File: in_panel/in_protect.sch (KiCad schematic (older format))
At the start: 8 parts

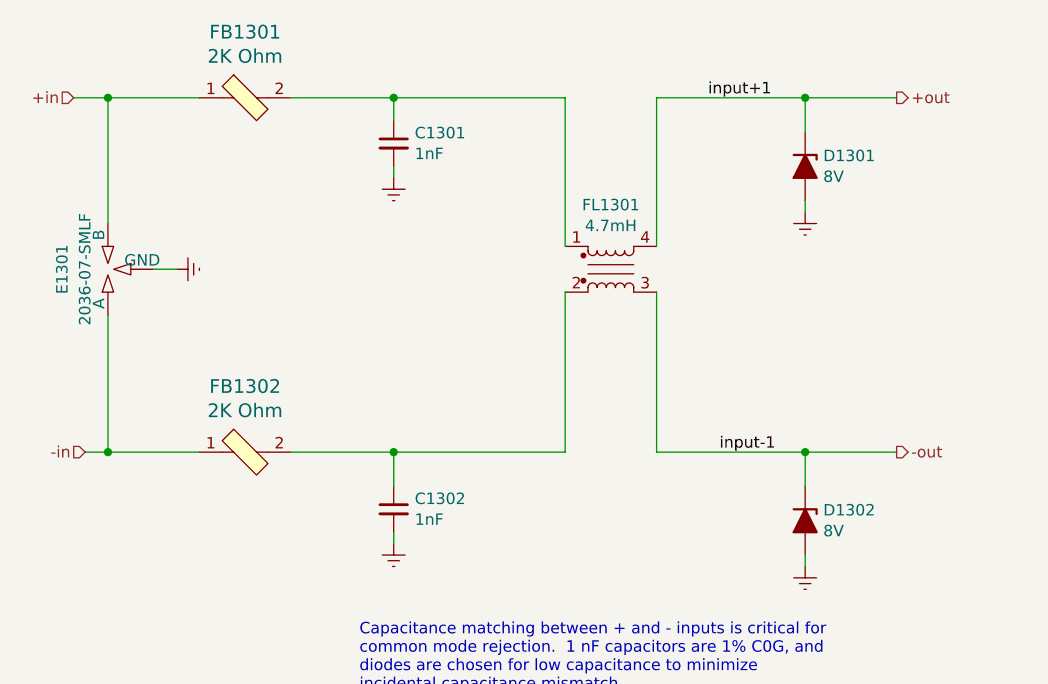
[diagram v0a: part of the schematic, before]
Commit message: More work on in_panel.  Also, shortened input_board by 10mm and tweaked the testpoints a bit, added another GND, and changed the supply TPs to be a hookable type.
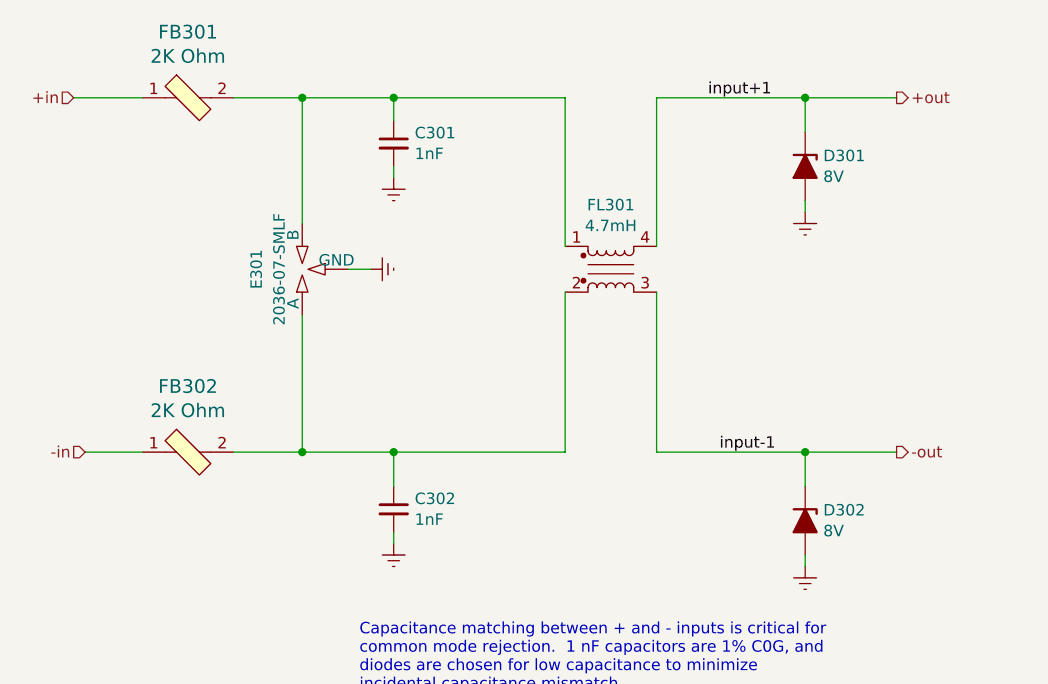
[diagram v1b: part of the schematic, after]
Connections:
- net +in: no longer E301.3 (B)
- net -in: no longer E301.1 (A)
- net at C301.1, FB301.2, FL301.1: now also E301.3 (B)
- net at C302.1, FB302.2, FL301.2: now also E301.1 (A)
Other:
- moved on the sheet: E301, FB301, FB302

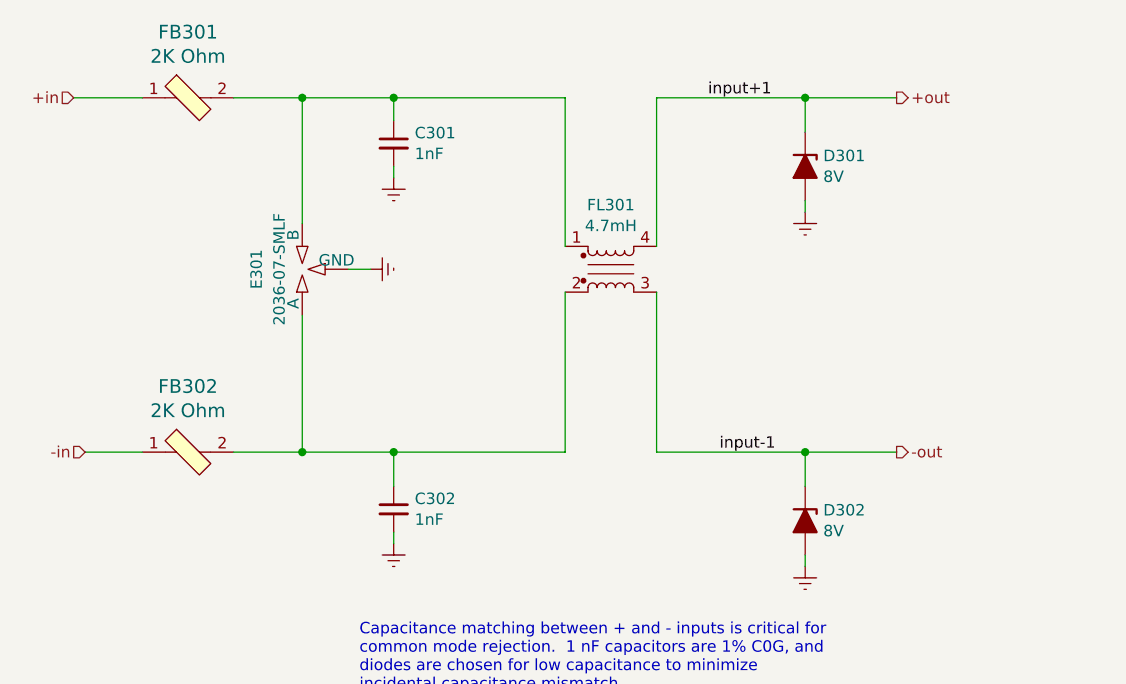
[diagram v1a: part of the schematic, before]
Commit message: in_panel is nearly complete, input/adc.sch: change testpoint style to loop. input/input_channel.sch: modification seems spurious
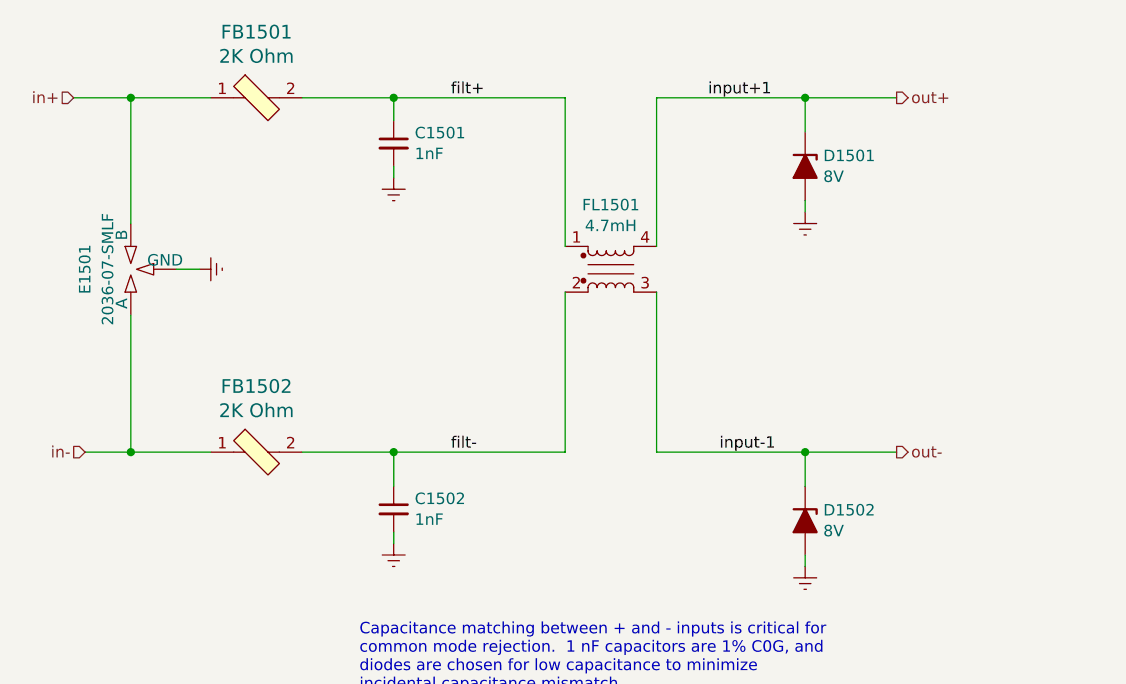
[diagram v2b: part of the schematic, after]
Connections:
- net filt+: now reaches C301.1, FB301.2, FL301.1
- net filt+: no longer E301.3 (B)
- net filt-: now reaches C302.1, FB302.2, FL301.2
- net filt-: no longer E301.1 (A)
- net +in renamed in+
- net in+: now also E301.3 (B)
- net +out renamed out+
- net -in renamed in-
- net in-: now also E301.1 (A)
- net -out renamed out-
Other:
- moved on the sheet: E1501, FB1501, FB1502

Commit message: Revision 0 of in_panel, off to fab
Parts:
- C301, C302: DK line 1 -> I.1
- D301, D302: DK line 58 -> I.58
- E301: DK line 8 -> I.8
- FB301, FB302: DK line 5 -> I.5
- FL301: DK line 6 -> I.6
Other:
- note added: "Input filter, first stage of transient/ESD protection. This first stage is\nreferenced to the chassis ground, while the input card filter and clamps are\nreferenced to the card's ground."
- note added: "The idea is to intercept ESD, surges, and RFI at the front panel, and then \npresent a high common mode output impedance to the input card.\nAside from protecting against damage, we also want to suppress any\nRFI that might be rectified at the amplifier input, especially in the\nrange of 1-100 MHz or so.\n\nThe sensor coil is a floating AC coupled input, and is biased to a\ncommon mode voltage of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"
- note removed: "Input filter, first stage of transient/ESD protection"
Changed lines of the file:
@@
 AR Path="/60030EFF/6001E836/5DE42B90" Ref="FB1401"  Part="1"
 AR Path="/60030EFF/6001E9CD/5DE42B90" Ref="FB1501"  Part="1"
-F 0 "FB1501" H 3150 2287 60  0000 C CNN
+F 0 "FB301" H 3150 2287 60  0000 C CNN
 F 1 "2K Ohm" H 3150 2181 60  0000 C CNN
 F 2 "Inductor_SMD:L_0805_2012Metric" H 3350 2200 60  0001 L CNN
@@
 F 11 "Laird-Signal Integrity Products" H 3350 3100 60  0001 L CNN "Manufacturer"
 F 12 "Active" H 3350 3200 60  0001 L CNN "Status"
-F 13 "5" H 3150 2000 50  0001 C CNN "DK line"
+F 13 "I.5" H 3150 2000 50  0001 C CNN "DK line"
 F 14 "240-2396-1-ND" H 3150 2000 50  0001 C CNN "Digikey"
 	1    3150 2000
@@
 AR Path="/60030EFF/6001E836/5DE46A26" Ref="C1401"  Part="1"
 AR Path="/60030EFF/6001E9CD/5DE46A26" Ref="C1501"  Part="1"
-F 0 "C1501" H 3842 2246 50  0000 L CNN
+F 0 "C301" H 3842 2246 50  0000 L CNN
 F 1 "1nF" H 3842 2155 50  0000 L CNN
 F 2 "Capacitor_SMD:C_0805_2012Metric" H 3750 2200 50  0001 C CNN
@@
 F 5 "CC0805FRNPO0BN102" H 3750 2200 50  0001 C CNN "MPN"
 F 6 "CAP CER 1000PF 100V NPO 0805" H 3750 2200 50  0001 C CNN "Description"
-F 7 "1" H 3750 2200 50  0001 C CNN "DK line"
+F 7 "I.1" H 3750 2200 50  0001 C CNN "DK line"
 F 8 "Yageo" H 3750 2200 50  0001 C CNN "Manufacturer"
 	1    3750 2200
@@
 AR Path="/60030EFF/6001E836/5E195561" Ref="FL1401"  Part="1"
 AR Path="/60030EFF/6001E9CD/5E195561" Ref="FL1501"  Part="1"
-F 0 "FL1501" H 4700 3031 50  0000 C CNN
+F 0 "FL301" H 4700 3031 50  0000 C CNN
 F 1 "4.7mH" H 4700 2940 50  0000 C CNN
 F 2 "input:L_CommonMode_Bourns_DR331" H 4700 2500 50  0001 C CNN
@@
 F 4 "DR331-475BECT-ND" H 4700 2750 50  0001 C CNN "Digikey"
 F 5 "DR331-475BE" H 4700 2750 50  0001 C CNN "MPN"
-F 6 "6" H 4700 2750 50  0001 C CNN "DK line"
+F 6 "I.6" H 4700 2750 50  0001 C CNN "DK line"
 F 7 "CMC 4.7MH 200MA 2LN SMD" H 4700 2750 50  0001 C CNN "Description"
 F 8 "Bourns Inc." H 4700 2750 50  0001 C CNN "Manufacturer"
@@
 AR Path="/60030EFF/6001E836/5DE4DC1A" Ref="FB1402"  Part="1"
 AR Path="/60030EFF/6001E9CD/5DE4DC1A" Ref="FB1502"  Part="1"
-F 0 "FB1502" H 3150 3837 60  0000 C CNN
+F 0 "FB302" H 3150 3837 60  0000 C CNN
 F 1 "2K Ohm" H 3150 3731 60  0000 C CNN
 F 2 "Inductor_SMD:L_0805_2012Metric" H 3350 3750 60  0001 L CNN
@@
 F 11 "Laird-Signal Integrity Products" H 3350 4650 60  0001 L CNN "Manufacturer"
 F 12 "Active" H 3350 4750 60  0001 L CNN "Status"
-F 13 "5" H 3150 3550 50  0001 C CNN "DK line"
+F 13 "I.5" H 3150 3550 50  0001 C CNN "DK line"
 F 14 "240-2396-1-ND" H 3150 3550 50  0001 C CNN "Digikey"
 	1    3150 3550
@@
 AR Path="/60030EFF/6001E836/5E195563" Ref="C1402"  Part="1"
 AR Path="/60030EFF/6001E9CD/5E195563" Ref="C1502"  Part="1"
-F 0 "C1502" H 3842 3846 50  0000 L CNN
+F 0 "C302" H 3842 3846 50  0000 L CNN
 F 1 "1nF" H 3842 3755 50  0000 L CNN
 F 2 "Capacitor_SMD:C_0805_2012Metric" H 3750 3800 50  0001 C CNN
@@
 F 5 "CC0805FRNPO0BN102" H 3750 3800 50  0001 C CNN "MPN"
 F 6 "CAP CER 1000PF 100V NPO 0805" H 3750 3800 50  0001 C CNN "Description"
-F 7 "1" H 3750 3800 50  0001 C CNN "DK line"
+F 7 "I.1" H 3750 3800 50  0001 C CNN "DK line"
 F 8 "Yageo" H 3750 3800 50  0001 C CNN "Manufacturer"
 	1    3750 3800
@@
 AR Path="/60030EFF/6001E836/5DE60CD7" Ref="D1401"  Part="1"
 AR Path="/60030EFF/6001E9CD/5DE60CD7" Ref="D1501"  Part="1"
-F 0 "D1501" V 5504 2379 50  0000 L CNN
+F 0 "D301" V 5504 2379 50  0000 L CNN
 F 1 "8V" V 5595 2379 50  0000 L CNN
 F 2 "Diode_SMD:D_SOD-323" H 5550 2300 50  0001 C CNN
@@
 F 4 "CDSOD323-T08LCT-ND" V 5550 2300 50  0001 C CNN "Digikey"
 F 5 "CDSOD323-T08L" V 5550 2300 50  0001 C CNN "MPN"
-F 6 "58" H 5550 2300 50  0001 C CNN "DK line"
+F 6 "I.58" H 5550 2300 50  0001 C CNN "DK line"
 F 7 "TVS DIODE 8V 18.3V SOD323" H 5550 2300 50  0001 C CNN "Description"
 F 8 "Bourns Inc." H 5550 2300 50  0001 C CNN "Manufacturer"
@@
 AR Path="/60030EFF/6001E836/5DE6E14A" Ref="D1402"  Part="1"
 AR Path="/60030EFF/6001E9CD/5DE6E14A" Ref="D1502"  Part="1"
-F 0 "D1502" V 5504 3929 50  0000 L CNN
+F 0 "D302" V 5504 3929 50  0000 L CNN
 F 1 "8V" V 5595 3929 50  0000 L CNN
 F 2 "Diode_SMD:D_SOD-323" H 5550 3850 50  0001 C CNN
@@
 F 4 "CDSOD323-T08LCT-ND" V 5550 3850 50  0001 C CNN "Digikey"
 F 5 "CDSOD323-T08L" V 5550 3850 50  0001 C CNN "MPN"
-F 6 "58" H 5550 3850 50  0001 C CNN "DK line"
+F 6 "I.58" H 5550 3850 50  0001 C CNN "DK line"
 F 7 "TVS DIODE 8V 18.3V SOD323" H 5550 3850 50  0001 C CNN "Description"
 F 8 "Bourns Inc." H 5550 3850 50  0001 C CNN "Manufacturer"
@@
 Wire Wire Line
 	5550 2150 5550 2000
-Text Notes 3600 4600 0    50   ~ 0
+Text Notes 6400 2950 0    50   ~ 0
 Capacitance matching between + and - inputs is critical for \ncommon mode rejection.  1 nF capacitors are 1% C0G, and\ndiodes are chosen for low capacitance to minimize\nincidental capacitance mismatch.
 Wire Wire Line
@@
 AR Path="/60030EFF/6001E836/5E376466" Ref="E1401"  Part="1"
 AR Path="/60030EFF/6001E9CD/5E376466" Ref="E1501"  Part="1"
-F 0 "E1501" H 2600 2950 50  0000 C CNN
+F 0 "E301" H 2600 2950 50  0000 C CNN
 F 1 "2036-07-SMLF" H 2600 2850 50  0000 C CNN
 F 2 "input:GDT_3LINE_Bourns_2036-xx-SM" H 2600 2680 50  0001 C CNN
@@
 F 4 "2036-07-SMLF-ND" H 2600 2750 50  0001 C CNN "Digikey"
 F 5 "GDT 75V 20% 10KA SURFACE MOUNT" H 2600 2750 50  0001 C CNN "Description"
-F 6 "8" H 2600 2750 50  0001 C CNN "DK line"
+F 6 "I.8" H 2600 2750 50  0001 C CNN "DK line"
 F 7 "2036-07-SMLF" H 2600 2750 50  0001 C CNN "MPN"
 F 8 "Bourns Inc." H 2600 2750 50  0001 C CNN "Manufacturer"
@@
 Text HLabel 5950 3550 2    50   Output ~ 0
 out-
-Text Notes 7050 6750 0    50   ~ 0
-Input filter, first stage of transient/ESD protection
+Text Notes 7250 6900 0    50   ~ 0
+Input filter, first stage of transient/ESD protection. This first stage is\nreferenced to the chassis ground, while the input card filter and clamps are\nreferenced to the card's ground.
 Wire Wire Line
 	3350 2000 3750 2000
@@
 Text Label 4000 3550 0    50   ~ 0
 filt-
+Text Notes 2950 5200 0    50   ~ 0
+The idea is to intercept ESD, surges, and RFI at the front panel, and then \npresent a high common mode output impedance to the input card.\nAside from protecting against damage, we also want to suppress any\nRFI that might be rectified at the amplifier input, especially in the\nrange of 1-100 MHz or so.\n\nThe sensor coil is a floating AC coupled input, and is biased to a\ncommon mode voltage of about 2.5V by the input card.  The input\nrange is nominally 0 to 5V, though the common mode range\nwill be somewhat wider.
 $EndSCHEMATC
